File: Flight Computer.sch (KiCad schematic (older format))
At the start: 24 parts, among them J1 Conn_01x08, U1 VXO7803-1000, U2 W25Q32JVSS, U3 W25Q32JVSS, U4 Adafruit_GPS_THT, U5 BMP280

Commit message: Annotated schematic Added 2N7002 packages Updated PCB
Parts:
- gave numbers to parts that had none: 8
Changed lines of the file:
@@
 $EndComp
-Wire Wire Line
-	4850 5200 4850 5250
 Wire Wire Line
 	2750 5200 2750 5250
@@
 NoConn ~ 4750 6300
 $Comp
-L power:+3V3 #PWR?
+L power:+3V3 #PWR0101
 U 1 1 5EDB252B
 P 2150 1800
-F 0 "#PWR?" H 2150 1650 50  0001 C CNN
+F 0 "#PWR0101" H 2150 1650 50  0001 C CNN
 F 1 "+3V3" H 2150 1940 50  0000 C CNN
 F 2 "" H 2150 1800 50  0001 C CNN
@@
 $EndComp
 $Comp
-L Device:R R?
+L Device:R R4
 U 1 1 5E1FF2AB
 P 1450 2200
-F 0 "R?" V 1530 2200 50  0000 C CNN
+F 0 "R4" V 1530 2200 50  0000 C CNN
 F 1 "100R" V 1450 2200 50  0000 C CNN
 F 2 "Resistor_SMD:R_1206_3216Metric_Pad1.42x1.75mm_HandSolder" V 1380 2200 50  0001 C CNN
@@
 	2150 1800 2150 2950
 $Comp
-L Device:C C?
+L Device:C C13
 U 1 1 5E2632E5
 P 3950 4350
-F 0 "C?" H 4000 4250 50  0000 L CNN
+F 0 "C13" H 4000 4250 50  0000 L CNN
 F 1 "0.1uF" H 3950 4450 50  0000 L CNN
 F 2 "Capacitor_SMD:C_0603_1608Metric_Pad1.05x0.95mm_HandSolder" H 3988 4200 50  0001 C CNN
@@
 $EndComp
 $Comp
-L Device:C C?
+L Device:C C12
 U 1 1 5E26A385
 P 3650 4350
-F 0 "C?" H 3700 4250 50  0000 L CNN
+F 0 "C12" H 3700 4250 50  0000 L CNN
 F 1 "0.1uF" H 3650 4450 50  0000 L CNN
 F 2 "Capacitor_SMD:C_0603_1608Metric_Pad1.05x0.95mm_HandSolder" H 3688 4200 50  0001 C CNN
@@
 $EndComp
 $Comp
-L Device:C C?
+L Device:C C14
 U 1 1 5E2718DF
 P 7000 2850
-F 0 "C?" H 7050 2750 50  0000 L CNN
+F 0 "C14" H 7050 2750 50  0000 L CNN
 F 1 "0.1uF" H 7000 2950 50  0000 L CNN
 F 2 "Capacitor_SMD:C_0603_1608Metric_Pad1.05x0.95mm_HandSolder" H 7038 2700 50  0001 C CNN
@@
 $EndComp
 $Comp
-L Device:C C?
+L Device:C C15
 U 1 1 5E278C33
 P 9950 1500
-F 0 "C?" H 10000 1400 50  0000 L CNN
+F 0 "C15" H 10000 1400 50  0000 L CNN
 F 1 "0.1uF" H 9950 1600 50  0000 L CNN
 F 2 "Capacitor_SMD:C_0603_1608Metric_Pad1.05x0.95mm_HandSolder" H 9988 1350 50  0001 C CNN
@@
 $EndComp
 $Comp
-L Device:C C?
+L Device:C C11
 U 1 1 5E27FBC9
 P 3450 1250
-F 0 "C?" H 3500 1150 50  0000 L CNN
+F 0 "C11" H 3500 1150 50  0000 L CNN
 F 1 "0.1uF" H 3450 1350 50  0000 L CNN
 F 2 "Capacitor_SMD:C_0603_1608Metric_Pad1.05x0.95mm_HandSolder" H 3488 1100 50  0001 C CNN
@@
 	4850 4150 4850 4400
 $Comp
-L power:GND #PWR?
+L power:GND #PWR0102
 U 1 1 5E2E8B8F
 P 3800 4600
-F 0 "#PWR?" H 3800 4350 50  0001 C CNN
+F 0 "#PWR0102" H 3800 4350 50  0001 C CNN
 F 1 "GND" H 3800 4450 50  0000 C CNN
 F 2 "" H 3800 4600 50  0001 C CNN
@@
 	7150 2650 7150 2950
 $Comp
-L power:GND #PWR?
+L power:GND #PWR0103
 U 1 1 5E365BF8
 P 7000 3050
-F 0 "#PWR?" H 7000 2800 50  0001 C CNN
+F 0 "#PWR0103" H 7000 2800 50  0001 C CNN
 F 1 "GND" H 7000 2900 50  0000 C CNN
 F 2 "" H 7000 3050 50  0001 C CNN
@@
 Connection ~ 9650 1800
 $Comp
-L power:GND #PWR?
+L power:GND #PWR0104
 U 1 1 5E3C53B8
 P 3450 1450
-F 0 "#PWR?" H 3450 1200 50  0001 C CNN
+F 0 "#PWR0104" H 3450 1200 50  0001 C CNN
 F 1 "GND" H 3450 1300 50  0000 C CNN
 F 2 "" H 3450 1450 50  0001 C CNN
@@
 Connection ~ 3700 1050
 $Comp
-L Device:C C?
+L Device:C C2
 U 1 1 5E3E020E
 P 950 1150
-F 0 "C?" H 1000 1050 50  0000 L CNN
+F 0 "C2" H 1000 1050 50  0000 L CNN
 F 1 "10uF" H 950 1250 50  0000 L CNN
 F 2 "Capacitor_SMD:C_1206_3216Metric_Pad1.42x1.75mm_HandSolder" H 988 1000 50  0001 C CNN
@@
 $EndComp
 $Comp
-L Device:C C?
+L Device:C C10
 U 1 1 5E3E9DF6
 P 2200 1150
-F 0 "C?" H 2250 1050 50  0000 L CNN
+F 0 "C10" H 2250 1050 50  0000 L CNN
 F 1 "10uF" H 2200 1250 50  0000 L CNN
 F 2 "Capacitor_SMD:C_1206_3216Metric_Pad1.42x1.75mm_HandSolder" H 2238 1000 50  0001 C CNN
@@
 Wire Wire Line
 	7150 5450 8150 5450
+Wire Wire Line
+	4850 5200 4850 5250
 Wire Bus Line
 	7400 5650 7400 6350

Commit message: All ERC errors gone
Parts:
- removed AC1: ADXL345, SamacSys_Parts:CC-14-1, symbol SamacSys_Parts:ADXL345
- removed C14: 0.1uF, Capacitor_SMD:C_0603_1608Metric_Pad1.05x0.95mm_HandSolder, symbol Device:C
- removed U5: BMP280, Package_LGA:Bosch_LGA-8_2x2.5mm_P0.65mm_ClockwisePinNumbering, symbol SamacSys_Parts:bmp280
- added U?: ADXL343, Package_LGA:LGA-14_3x5mm_P0.8mm_LayoutBorder1x6y, symbol Sensor_Motion:ADXL343
- added U?: BMP280, Package_LGA:Bosch_LGA-8_2x2.5mm_P0.65mm_ClockwisePinNumbering, symbol Sensor_Pressure:BMP280
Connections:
- wire segments 170 -> 157
- no-connect marks 35 -> 34
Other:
- moved on the sheet: C11, C15

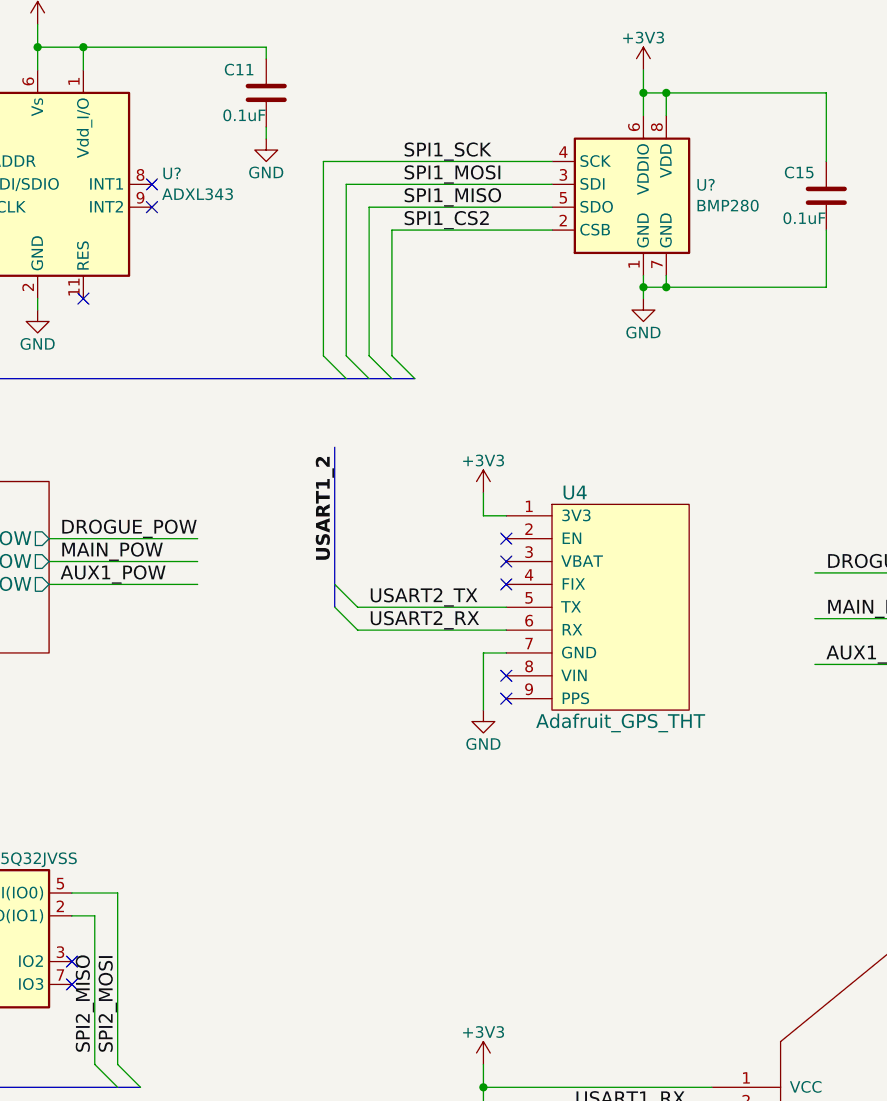
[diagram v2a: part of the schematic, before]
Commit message: GPS module power fixed
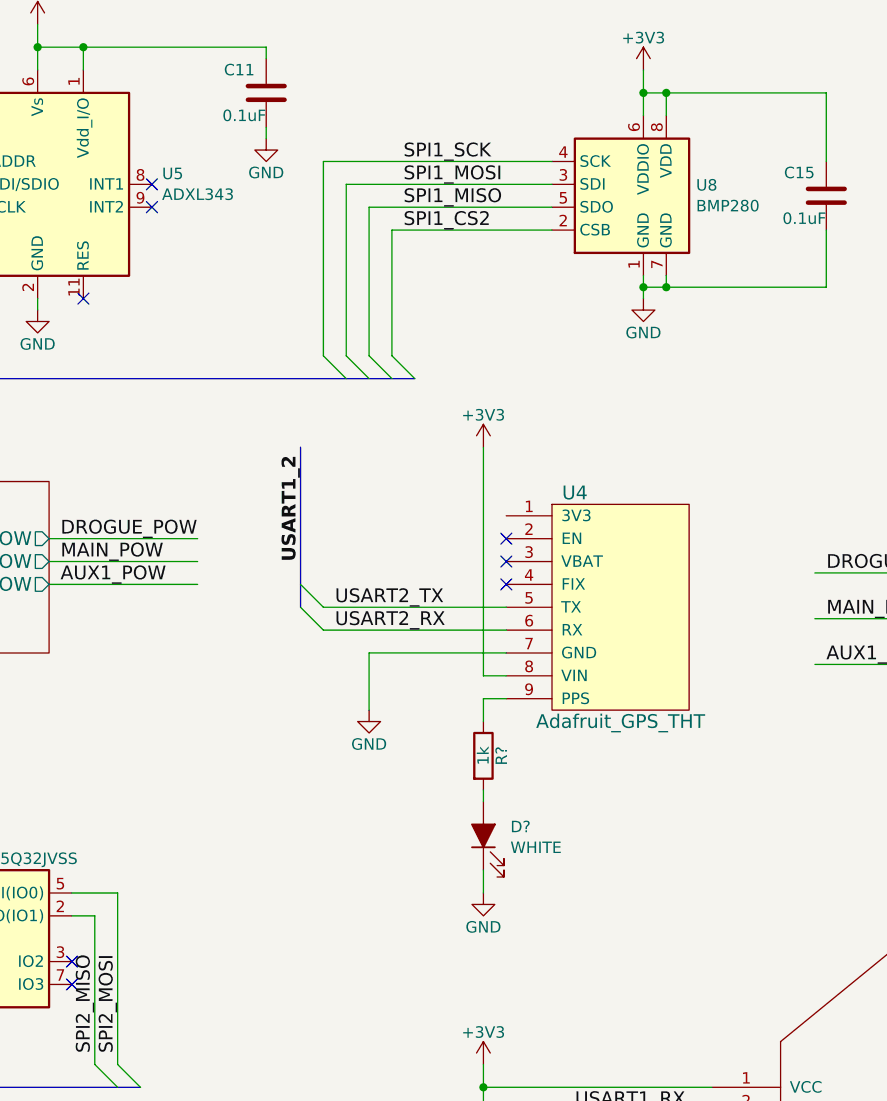
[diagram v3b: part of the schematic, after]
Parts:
- added D?: WHITE, LED_SMD:LED_0603_1608Metric_Pad1.05x0.95mm_HandSolder, symbol Device:LED_ALT
- added R?: 1k, Resistor_SMD:R_1206_3216Metric_Pad1.42x1.75mm_HandSolder, symbol Device:R
- gave numbers to parts that had none: 2
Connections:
- wire segments 157 -> 161
- no-connect marks 34 -> 32
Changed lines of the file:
@@
 	1    0    0    -1
 $EndComp
-NoConn ~ 7250 3650
 $Comp
 L power:+3V3 #PWR020
 U 1 1 5AE652C6
-P 7150 2850
-F 0 "#PWR020" H 7150 2700 50  0001 C CNN
-F 1 "+3V3" H 7150 2990 50  0000 C CNN
-F 2 "" H 7150 2850 50  0001 C CNN
-F 3 "" H 7150 2850 50  0001 C CNN
-	1    7150 2850
-	1    0    0    -1
-$EndComp
-NoConn ~ 7250 3750
+P 7150 2650
+F 0 "#PWR020" H 7150 2500 50  0001 C CNN
+F 1 "+3V3" H 7150 2790 50  0000 C CNN
+F 2 "" H 7150 2650 50  0001 C CNN
+F 3 "" H 7150 2650 50  0001 C CNN
+	1    7150 2650
+	1    0    0    -1
+$EndComp
 NoConn ~ 7250 3250
 NoConn ~ 7250 3150
 NoConn ~ 7250 3050
 Wire Wire Line
-	7150 3550 7250 3550
-Wire Wire Line
-	7150 3800 7150 3550
+	6650 3800 6650 3550
 $Comp
 L Flight-Computer:Adafruit_GPS_THT U4
@@
 L power:GND #PWR021
 U 1 1 59C6A1E1
-P 7150 3800
-F 0 "#PWR021" H 7150 3550 50  0001 C CNN
-F 1 "GND" H 7150 3650 50  0000 C CNN
-F 2 "" H 7150 3800 50  0001 C CNN
-F 3 "" H 7150 3800 50  0001 C CNN
-	1    7150 3800
+P 6650 3800
+F 0 "#PWR021" H 6650 3550 50  0001 C CNN
+F 1 "GND" H 6650 3650 50  0000 C CNN
+F 2 "" H 6650 3800 50  0001 C CNN
+F 3 "" H 6650 3800 50  0001 C CNN
+	1    6650 3800
 	1    0    0    -1
 $EndComp
@@
 USART1_2
 Entry Wire Line
-	6500 3350 6600 3450
-Entry Wire Line
-	6500 3250 6600 3350
-Text Label 6650 3350 0    60   ~ 0
+	6350 3350 6450 3450
+Entry Wire Line
+	6350 3250 6450 3350
+Text Label 6500 3350 0    60   ~ 0
 USART2_TX
-Text Label 6650 3450 0    60   ~ 0
+Text Label 6500 3450 0    60   ~ 0
 USART2_RX
-Wire Wire Line
-	6600 3350 7250 3350
-Wire Wire Line
-	6600 3450 7250 3450
-Text Label 6500 3150 1    60   ~ 12
+Text Label 6350 3150 1    60   ~ 12
 USART1_2
 Wire Wire Line
@@
 Entry Wire Line
 	4250 5350 4350 5450
-Wire Wire Line
-	7150 2950 7250 2950
 Wire Wire Line
 	3950 2900 3400 2900
@@
 	4850 5200 4850 5250
 $Comp
-L Sensor_Motion:ADXL343 U?
+L Sensor_Motion:ADXL343 U5
 U 1 1 5EA124E2
 P 5200 1500
-F 0 "U?" H 5744 1546 50  0000 L CNN
+F 0 "U5" H 5744 1546 50  0000 L CNN
 F 1 "ADXL343" H 5744 1455 50  0000 L CNN
 F 2 "Package_LGA:LGA-14_3x5mm_P0.8mm_LayoutBorder1x6y" H 5200 1500 50  0001 C CNN
@@
 $EndComp
 $Comp
-L Sensor_Pressure:BMP280 U?
+L Sensor_Pressure:BMP280 U8
 U 1 1 5EA13F78
 P 7850 1600
-F 0 "U?" H 8080 1696 50  0000 L CNN
+F 0 "U8" H 8080 1696 50  0000 L CNN
 F 1 "BMP280" H 8080 1605 50  0000 L CNN
 F 2 "Package_LGA:Bosch_LGA-8_2x2.5mm_P0.65mm_ClockwisePinNumbering" H 7850 900 50  0001 C CNN
@@
 $EndComp
 $Comp
-L power:PWR_FLAG #FLG?
+L power:PWR_FLAG #FLG0101
 U 1 1 5EA1697F
 P 2450 2250
-F 0 "#FLG?" H 2450 2325 50  0001 C CNN
+F 0 "#FLG0101" H 2450 2325 50  0001 C CNN
 F 1 "PWR_FLAG" H 2450 2400 50  0000 C CNN
 F 2 "" H 2450 2250 50  0001 C CNN
@@
 $EndComp
 $Comp
-L power:GND #PWR?
+L power:GND #PWR0103
 U 1 1 5EA21106
 P 2450 2300
-F 0 "#PWR?" H 2450 2050 50  0001 C CNN
+F 0 "#PWR0103" H 2450 2050 50  0001 C CNN
 F 1 "GND" H 2450 2150 50  0000 C CNN
 F 2 "" H 2450 2300 50  0001 C CNN
@@
 Wire Wire Line
 	2450 2250 2450 2300
-Wire Wire Line
-	7150 2850 7150 2950
 NoConn ~ 5700 1500
 NoConn ~ 5700 1600
@@
 NoConn ~ 5000 1000
 $Comp
-L power:+3V3 #PWR?
+L power:+3V3 #PWR0113
 U 1 1 5EA77FDB
 P 5200 800
-F 0 "#PWR?" H 5200 650 50  0001 C CNN
+F 0 "#PWR0113" H 5200 650 50  0001 C CNN
 F 1 "+3V3" H 5200 940 50  0000 C CNN
 F 2 "" H 5200 800 50  0001 C CNN
@@
 	5200 900  5200 1000
 $Comp
-L power:GND #PWR?
+L power:GND #PWR0114
 U 1 1 5EA934F9
 P 5200 2050
-F 0 "#PWR?" H 5200 1800 50  0001 C CNN
+F 0 "#PWR0114" H 5200 1800 50  0001 C CNN
 F 1 "GND" H 5200 1900 50  0000 C CNN
 F 2 "" H 5200 2050 50  0001 C CNN
@@
 	4100 1700 4700 1700
 $Comp
-L power:+3V3 #PWR?
+L power:+3V3 #PWR0115
 U 1 1 5EC107A7
 P 7850 1000
-F 0 "#PWR?" H 7850 850 50  0001 C CNN
+F 0 "#PWR0115" H 7850 850 50  0001 C CNN
 F 1 "+3V3" H 7850 1140 50  0000 C CNN
 F 2 "" H 7850 1000 50  0001 C CNN
@@
 	7850 1100 7850 1200
 $Comp
-L power:GND #PWR?
+L power:GND #PWR0116
 U 1 1 5EC2969B
 P 7850 2000
-F 0 "#PWR?" H 7850 1750 50  0001 C CNN
+F 0 "#PWR0116" H 7850 1750 50  0001 C CNN
 F 1 "GND" H 7850 1850 50  0000 C CNN
 F 2 "" H 7850 2000 50  0001 C CNN
@@
 Wire Wire Line
 	6650 1600 7450 1600
+Wire Wire Line
+	6650 3550 7250 3550
+Wire Wire Line
+	7250 3650 7150 3650
+Wire Wire Line
+	6450 3350 7250 3350
+Wire Wire Line
+	6450 3450 7250 3450
+Wire Wire Line
+	7150 2650 7150 3650
+$Comp
+L Device:R R?
+U 1 1 5EDB17CF
+P 7150 4000
+F 0 "R?" V 7230 4000 50  0000 C CNN
+F 1 "1k" V 7150 4000 50  0000 C CNN
+F 2 "Resistor_SMD:R_1206_3216Metric_Pad1.42x1.75mm_HandSolder" V 7080 4000 50  0001 C CNN
+F 3 "" H 7150 4000 50  0001 C CNN
+	1    7150 4000
+	1    0    0    -1
+$EndComp
+$Comp
+L Device:LED_ALT D?
+U 1 1 5EDB17D5
+P 7150 4350
+AR Path="/5E1357AF/5EDB17D5" Ref="D?"  Part="1"
+AR Path="/5EDB17D5" Ref="D?"  Part="1"
+F 0 "D?" V 7189 4232 50  0000 R CNN
+F 1 "WHITE" V 7098 4232 50  0000 R CNN
+F 2 "LED_SMD:LED_0603_1608Metric_Pad1.05x0.95mm_HandSolder" H 7150 4350 50  0001 C CNN
+F 3 "~" H 7150 4350 50  0001 C CNN
+	1    7150 4350
+	0    -1   -1   0
+$EndComp
+Wire Wire Line
+	7150 4200 7150 4150
+$Comp
+L power:GND #PWR?
+U 1 1 5EDB925F
+P 7150 4600
+F 0 "#PWR?" H 7150 4350 50  0001 C CNN
+F 1 "GND" H 7150 4450 50  0000 C CNN
+F 2 "" H 7150 4600 50  0001 C CNN
+F 3 "" H 7150 4600 50  0001 C CNN
+	1    7150 4600
+	1    0    0    -1
+$EndComp
+Wire Wire Line
+	7150 4500 7150 4600
+Wire Wire Line
+	7250 3750 7150 3750
+Wire Wire Line
+	7150 3750 7150 3850
 Wire Bus Line
 	7400 5650 7400 6350
@@
 	1450 7400 1450 7800
 Wire Bus Line
-	6500 2650 6500 3350
+	6350 2650 6350 3350
 Wire Bus Line
 	3300 3150 3300 3700
